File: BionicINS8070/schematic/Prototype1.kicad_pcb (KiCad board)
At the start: 2 copper layers, 48.3 x 71.1 mm, 8 parts, among them J1 BionicConnector, U1 INS8070, U2 74HCT126

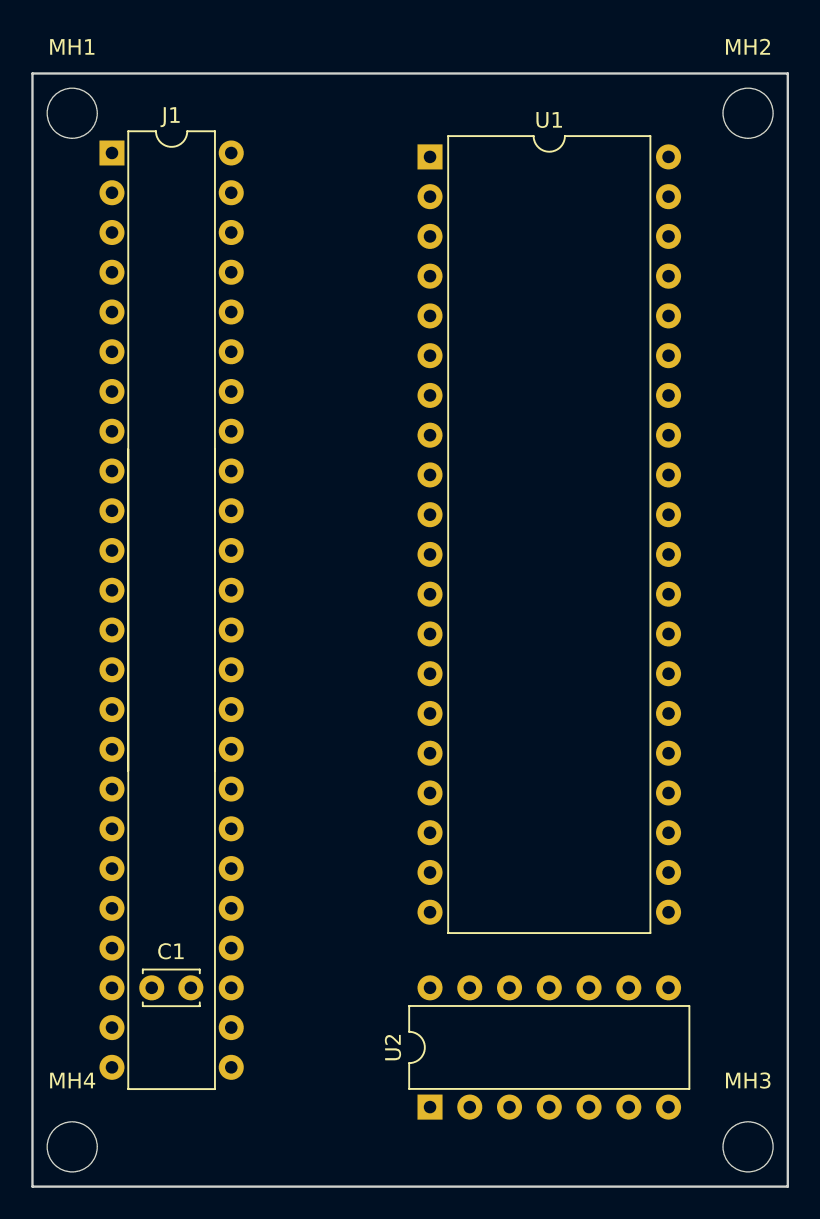
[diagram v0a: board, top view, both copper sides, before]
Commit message: Fix Bionic connector pin outs
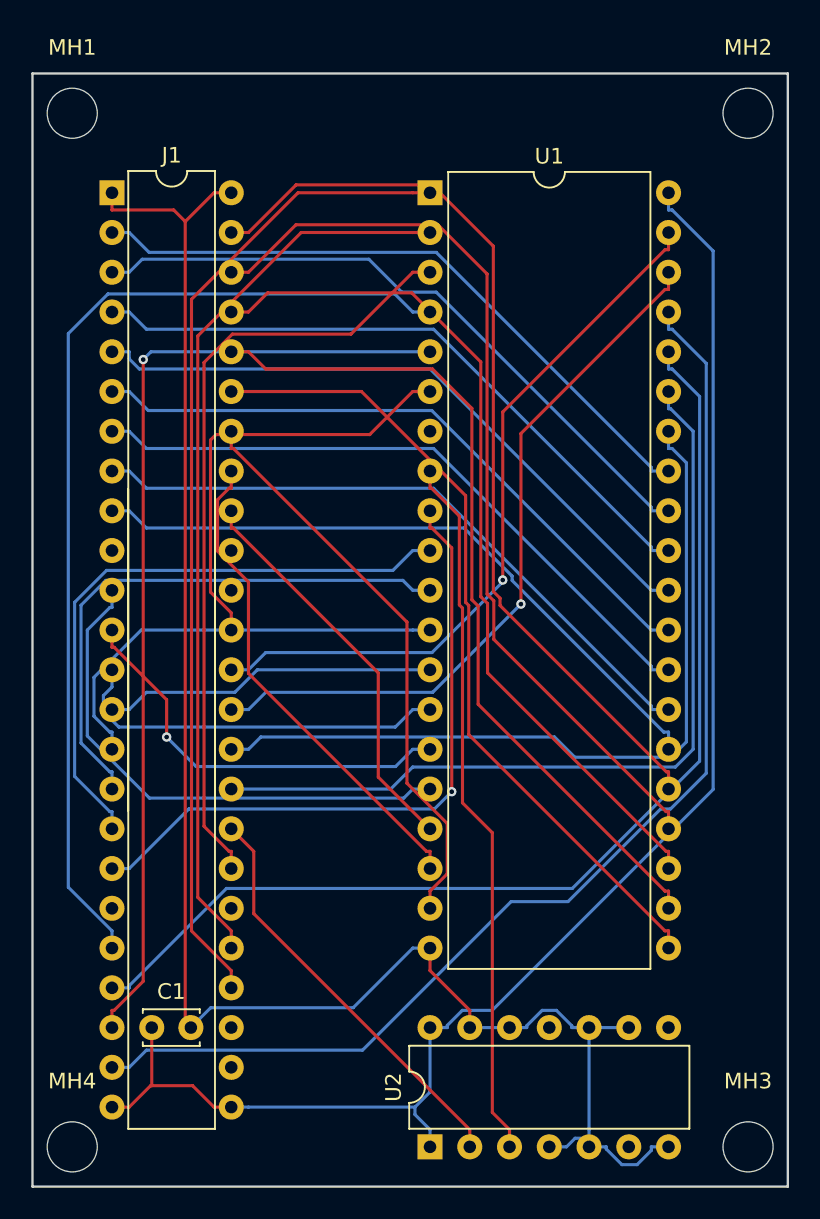
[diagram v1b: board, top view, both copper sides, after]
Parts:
- moved C1 2.54 mm to (106.1, 128.4)
- moved J1 2.54 mm to (103.5, 75.1)
- moved U2 2.54 mm to (123.9, 136.0)
- moved U1 2.29 mm to (123.9, 75.1)
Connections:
- J1 pad 11: /P20 -> /P30
- J1 pad 12: /P21 -> /P31
- J1 pad 13: /P22 -> /P32
- J1 pad 14: /P23 -> /P33
- J1 pad 15: /P24 -> /P34
- J1 pad 16: /P25 -> /P35
- J1 pad 17: /P26 -> /P36
- J1 pad 18: /P27 -> /P37
- J1 pad 40: /P37 -> /P27
- J1 pad 41: /P36 -> /P26
- J1 pad 42: /P35 -> /P25
- J1 pad 43: /P34 -> /P24
- J1 pad 44: /P33 -> /P23
- J1 pad 45: /P32 -> /P22
- J1 pad 46: /P31 -> /P21
- J1 pad 47: /P30 -> /P20
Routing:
- net GND: track 0.00 -> 112.8 mm
- net VCC: track 0.00 -> 96.5 mm
- net /P53: track 0.00 -> 76.4 mm
- net /P51: track 0.00 -> 70.7 mm
- net /P50: track 0.00 -> 65.1 mm
- net /P55: track 0.00 -> 63.1 mm
- net /P52: track 0.00 -> 62.1 mm, vias 0 -> 1
- net /P21: track 0.00 -> 59.3 mm
- net /P20: track 0.00 -> 59.0 mm
- net /P54: track 0.00 -> 57.6 mm
- net /P22: track 0.00 -> 55.7 mm
- net /P23: track 0.00 -> 54.2 mm
- net /P45: track 0.00 -> 54.2 mm
- net /P24: track 0.00 -> 52.1 mm
- net /P44: track 0.00 -> 50.8 mm
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
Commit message: Migrate to KiCad 6.0
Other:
- net class Default removed
